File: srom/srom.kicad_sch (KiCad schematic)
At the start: 22 parts, among them J1 Conn_01x03_Female, Q1 PN2222A, U1 4075, U2 74LS245, U3 74LS245, U4 74LS245, U5 Pico-1 ROM

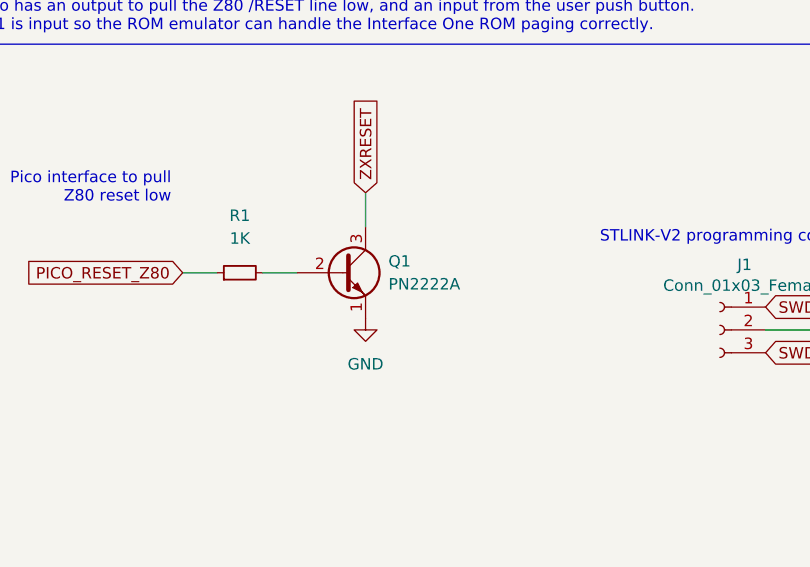
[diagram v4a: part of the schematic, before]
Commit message: fix 2222 transistor footprint on PCB
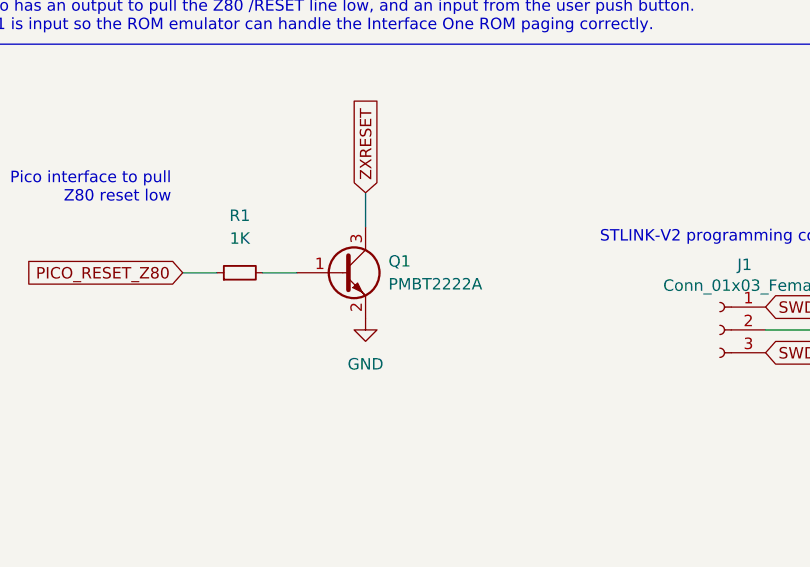
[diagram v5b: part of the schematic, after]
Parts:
- removed Q1: PN2222A, Package_TO_SOT_SMD:SOT-23-3, symbol Transistor_BJT:PN2222A
- added Q1: PMBT2222A, Package_TO_SOT_SMD:TSOT-23_HandSoldering, symbol 2222 SMD:PMBT2222A
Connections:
- net GND: now also Q1.2 (E)
- net ZXRESET: now also Q1.3 (C)
- net at R1.2: now also Q1.1 (B)
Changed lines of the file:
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@@
     (pin "2")
-  )
-  (symbol (lib_id "Transistor_BJT:PN2222A") (at 217.17 151.13 0) (unit 1)
-    (in_bom yes) (on_board yes) (fields_autoplaced)
-    (property "Reference" "Q1" (id 0) (at 222.25 149.8599 0)
-      (effects (font (size 1.27 1.27)) (justify left))
-    )
-    (property "Value" "PN2222A" (id 1) (at 222.25 152.3999 0)
-      (effects (font (size 1.27 1.27)) (justify left))
-    )
-    (property "Footprint" "Package_TO_SOT_SMD:SOT-23-3" (id 2) (at 222.25 153.035 0)
-      (effects (font (size 1.27 1.27) italic) (justify left) hide)
-    )
-    (property "Datasheet" "https://www.onsemi.com/pub/Collateral/PN2222-D.PDF" (id 3) (at 217.17 151.13 0)
-      (effects (font (size 1.27 1.27)) (justify left) hide)
-    )
-    (pin "1")
-    (pin "2")
-    (pin "3")
   )
   (symbol (lib_id "4xxx:4075") (at 93.98 27.94 270) (mirror x) (unit 4)
@@
     (pin "1")
   )
+  (symbol (lib_id "2222 SMD:PMBT2222A") (at 217.17 151.13 0) (unit 1)
+    (in_bom yes) (on_board yes) (fields_autoplaced)
+    (property "Reference" "Q1" (id 0) (at 222.25 149.8599 0)
+      (effects (font (size 1.27 1.27)) (justify left))
+    )
+    (property "Value" "PMBT2222A" (id 1) (at 222.25 152.3999 0)
+      (effects (font (size 1.27 1.27)) (justify left))
+    )
+    (property "Footprint" "Package_TO_SOT_SMD:TSOT-23_HandSoldering" (id 2) (at 222.25 153.035 0)
+      (effects (font (size 1.27 1.27) italic) (justify left) hide)
+    )
+    (property "Datasheet" "https://www.mouser.co.uk/ProductDetail/771-PMBT2222A-T-R" (id 3) (at 217.17 151.13 0)
+      (effects (font (size 1.27 1.27)) (justify left) hide)
+    )
+    (pin "1")
+    (pin "2")
+    (pin "3")
+  )
   (symbol (lib_id "Device:R") (at 72.39 125.73 90) (unit 1)
     (in_bom yes) (on_board yes) (fields_autoplaced)
@@
       (reference "J303") (unit 1) (value "Conn_01x03_Female") (footprint "Connector_PinHeader_2.54mm:PinHeader_1x03_P2.54mm_Vertical")
     )
-    (path "/1f0eb14f-70f5-4cb1-a65b-a81ba69b9e8d"
-      (reference "Q1") (unit 1) (value "PN2222A") (footprint "Package_TO_SOT_SMD:SOT-23-3")
+    (path "/e33c0819-efed-4286-8863-9252958751f9"
+      (reference "Q1") (unit 1) (value "PMBT2222A") (footprint "Package_TO_SOT_SMD:TSOT-23_HandSoldering")
     )
     (path "/bf2f21de-f445-4e9c-86ad-edabdf2b112f"
